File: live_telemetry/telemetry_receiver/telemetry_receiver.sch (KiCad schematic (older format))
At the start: 21 parts, among them J1 Conn_Coaxial, J2 Programming Header, J3 USB_A, U1 PIC16LF1455, U2 RFM95W, U3 AP2114H-3.3

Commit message: Add initial PCB layouts
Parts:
- J1: footprint (none) -> canhw_footprints:AmphenolRF_coaxial_conn_901-10510-2
- R5: footprint (none) -> Resistor_SMD:R_0805_2012Metric_Pad1.15x1.40mm_HandSolder
- U1: footprint (none) -> Package_SO:SOIC-14_3.9x8.7mm_P1.27mm
- U2: footprint (none) -> canhw_footprints:XCVR_RFM95W-915S2
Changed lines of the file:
@@
 F 0 "U1" H 4675 5115 50  0000 C CNN
 F 1 "PIC16LF1455" H 4675 5024 50  0000 C CNN
-F 2 "" H 4450 4800 50  0001 C CNN
+F 2 "Package_SO:SOIC-14_3.9x8.7mm_P1.27mm" H 4450 4800 50  0001 C CNN
 F 3 "http://ww1.microchip.com/downloads/en/DeviceDoc/40001639B.pdf" H 4450 4800 50  0001 C CNN
 	1    4450 4800
@@
 F 0 "U2" H 9000 4665 50  0000 C CNN
 F 1 "RFM95W" H 9000 4574 50  0000 C CNN
-F 2 "" H 8550 4550 50  0001 C CNN
+F 2 "canhw_footprints:XCVR_RFM95W-915S2" H 8550 4550 50  0001 C CNN
 F 3 "https://www.rfsolutions.co.uk/downloads/1463993415RFM95_96_97_98W.pdf" H 8550 4550 50  0001 C CNN
 	1    8500 3150
@@
 F 0 "J1" V 9782 2450 50  0000 L CNN
 F 1 "Conn_Coaxial" V 9873 2450 50  0000 L CNN
-F 2 "" H 9900 2350 50  0001 C CNN
+F 2 "canhw_footprints:AmphenolRF_coaxial_conn_901-10510-2" H 9900 2350 50  0001 C CNN
 F 3 " ~" H 9900 2350 50  0001 C CNN
 	1    9900 2350
@@
 F 0 "R5" H 3218 5396 50  0000 L CNN
 F 1 "10k" H 3218 5305 50  0000 L CNN
-F 2 "" V 3190 5340 50  0001 C CNN
+F 2 "Resistor_SMD:R_0805_2012Metric_Pad1.15x1.40mm_HandSolder" V 3190 5340 50  0001 C CNN
 F 3 "~" H 3150 5350 50  0001 C CNN
 	1    3150 5350

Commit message: Address Aaron's comments on initial component layout
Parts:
- J1: footprint canhw_footprints:AmphenolRF_coaxial_conn_901-10510-2 -> canhw_footprints:RF_connector_SMA_3-1478978-1
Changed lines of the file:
@@
 F 0 "J1" V 9782 2450 50  0000 L CNN
 F 1 "Conn_Coaxial" V 9873 2450 50  0000 L CNN
-F 2 "canhw_footprints:AmphenolRF_coaxial_conn_901-10510-2" H 9900 2350 50  0001 C CNN
+F 2 "canhw_footprints:RF_connector_SMA_3-1478978-1" H 9900 2350 50  0001 C CNN
 F 3 " ~" H 9900 2350 50  0001 C CNN
 	1    9900 2350

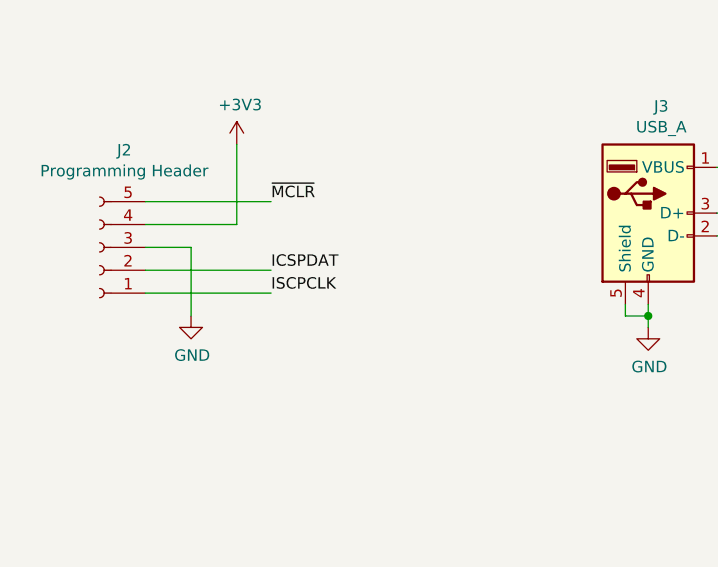
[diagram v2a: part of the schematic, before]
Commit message: Add initial trace routing
Note:
-LED colours still need to be added
-Waterloo Rocketry logo needs to be added with the board name and
my name on the right side of the board
-Copper pours will be added next commit
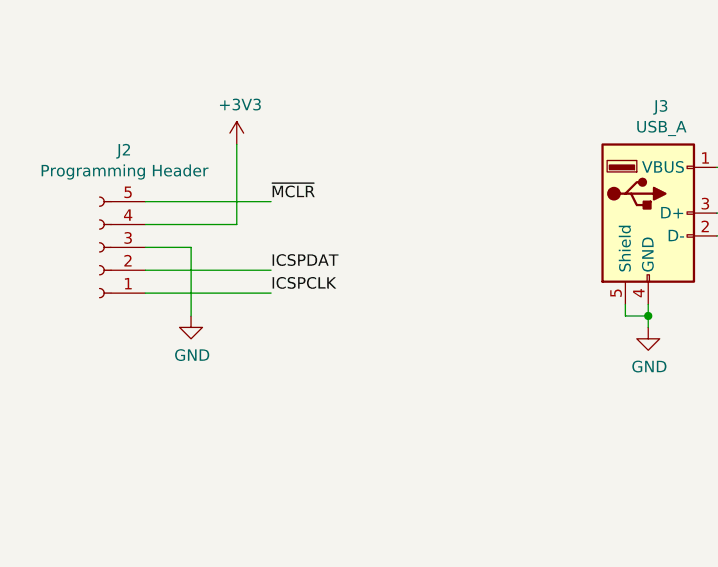
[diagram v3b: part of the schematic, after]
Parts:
- J2: footprint Connector_PinHeader_2.54mm:PinHeader_1x05_P2.54mm_Horizontal -> Connector_PinSocket_2.54mm:PinSocket_1x05_P2.54mm_Horizontal
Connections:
- net labels removed: ISCPCLK
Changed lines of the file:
@@
 F 0 "J2" H 1792 1875 50  0000 C CNN
 F 1 "Programming Header" H 1792 1966 50  0000 C CNN
-F 2 "Connector_PinHeader_2.54mm:PinHeader_1x05_P2.54mm_Horizontal" H 1900 2300 50  0001 C CNN
+F 2 "Connector_PinSocket_2.54mm:PinSocket_1x05_P2.54mm_Horizontal" H 1900 2300 50  0001 C CNN
 F 3 "~" H 1900 2300 50  0001 C CNN
 	1    1900 2300
@@
 ICSPDAT
 Text Label 2650 2500 0    50   ~ 0
-ISCPCLK
+ICSPCLK
 Wire Wire Line
 	2650 2500 2100 2500

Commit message: Remove old/replaced components for LTT and LTR
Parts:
- removed U1: PIC16LF1455, Package_SO:SOIC-14_3.9x8.7mm_P1.27mm, symbol canhw:PIC16F1455
- removed U2: RFM95W, canhw_footprints:XCVR_RFM95W-915S2, symbol canhw:RFM95W
- removed U3: AP2114H-3.3, Package_TO_SOT_SMD:SOT-23-5_HandSoldering, symbol Regulator_Linear:AP2112K-3.3
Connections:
- no-connect marks 6 -> 0

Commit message: Add LTR PIC and update LTR LDO
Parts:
- removed C2: 0.1u, Capacitor_SMD:C_0805_2012Metric_Pad1.15x1.40mm_HandSolder, symbol Device:C
- removed C4: 0.47u, Capacitor_SMD:C_0805_2012Metric_Pad1.15x1.40mm_HandSolder, symbol Device:C
- removed R5: 10k, Resistor_SMD:R_0805_2012Metric_Pad1.15x1.40mm_HandSolder, symbol Device:R_US
- added U?: PIC18F97J94, symbol canhw:PIC18F97J94
- added U?: NCV8114ASN330T1G, Package_TO_SOT_SMD:TSOT-23-5, symbol Regulator_Linear:NCV8114ASN330T1G
- C5, C6: value 4.7u -> 1u
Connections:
- net labels added: +3.3V
- wire segments 88 -> 81
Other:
- note removed: "NOTE: The MOSI and SCK SPI lines are sharing pins 9 and 10 with ICSPCLK and ICSPDAT. \nThis will prevent the board from using the PIC in-circuit debugging and sending data over\nserial at the same time. However, this solution is currently being used by USB board, and is\nwhat is recommended to be done in order to communicate with SPI with this specific PIC chip."
- moved on the sheet: C1, C3, C5, C6, D1, D2, D3, J2, J3, R1, R2, R3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

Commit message: Remove unused parts from LTS and add in new LTR MCU
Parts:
- removed AE1: Antenna, symbol Device:Antenna
- removed C1: 100p, Capacitor_SMD:C_0805_2012Metric_Pad1.15x1.40mm_HandSolder, symbol Device:C
- removed C3: 0.1u, Capacitor_SMD:C_0805_2012Metric_Pad1.15x1.40mm_HandSolder, symbol Device:C
- removed C5, C6: 1u, Capacitor_SMD:C_0805_2012Metric_Pad1.15x1.40mm_HandSolder, symbol Device:C
- removed J1: Conn_Coaxial, canhw_footprints:RF_connector_SMA_3-1478978-1, symbol Connector:Conn_Coaxial
- removed J3: USB_A, Connector_USB:USB_A_CNCTech_1001-011-01101_Horizontal, symbol Connector:USB_A
- removed U?: NCV8114ASN330T1G, Package_TO_SOT_SMD:TSOT-23-5, symbol Regulator_Linear:NCV8114ASN330T1G
- added C? (x2): C, symbol Device:C
- added Y?: Crystal, symbol Device:Crystal
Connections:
- net labels added: OSC1, OSC2
- net labels removed: +5V, MISO, MOSI, RESET, SCK, ~SS
- wire segments 81 -> 50
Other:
- moved on the sheet: D1, D2, D3, J2, R1, R2, R3, R4

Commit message: Add radios and label LTT and LTR
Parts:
- added C? (x2): 1u, Capacitor_SMD:C_0805_2012Metric_Pad1.15x1.40mm_HandSolder, symbol Device:C
- added C? (x2): 0.1uF, symbol Device:C
- added J?: USB_A, Connector_USB:USB_A_CNCTech_1001-011-01101_Horizontal, symbol Connector:USB_A
- added U?: ?, Package_TO_SOT_SMD:TSOT-23-5, symbol Regulator_Linear:NCV8114ASN330T1G
- C? (x2): value C -> 27pF
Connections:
- net labels added: +5V
- net labels removed: VUSB3V3
- wire segments 50 -> 79
- no-connect marks 0 -> 40
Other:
- note added: "12 MHz CRYSTAL"
- note added: "5V to 3.3V VOLTAGE REGULATOR"
- note added: "DEBUG LEDS"
- note added: "MCU"
- note added: "PROGRAMMING HEADER"
- note added: "USB CONNECTOR"
- moved on the sheet: J2

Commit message: Add placeholder LDOs for LTT and LTR
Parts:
- C? (x2): value 1u -> 1uF
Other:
- note added: "Note: The actual voltage regulator part # has not been selected yet. TBD ASAP."
- note added: "Note: This PIC has lots of unused pins,\nbut not many PICs had USB support. \nThis PIC also has CAN support for \npotential future CAN debugging on LTR."
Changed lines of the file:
@@
 encoding utf-8
 Sheet 1 2
-Title ""
-Date ""
-Rev ""
+Title "Live Telemetry Receiver"
+Date "2021-09-27"
+Rev "2.0"
 Comp ""
 Comment1 ""
@@
 AR Path="/6109AF45/61564D33" Ref="C?"  Part="1"
 F 0 "C?" H 9065 3646 50  0000 L CNN
-F 1 "1u" H 9065 3555 50  0000 L CNN
+F 1 "1uF" H 9065 3555 50  0000 L CNN
 F 2 "Capacitor_SMD:C_0805_2012Metric_Pad1.15x1.40mm_HandSolder" H 8988 3450 50  0001 C CNN
 F 3 "~" H 8950 3600 50  0001 C CNN
@@
 AR Path="/6109AF45/61564D39" Ref="C?"  Part="1"
 F 0 "C?" H 10665 3646 50  0000 L CNN
-F 1 "1u" H 10665 3555 50  0000 L CNN
+F 1 "1uF" H 10665 3555 50  0000 L CNN
 F 2 "Capacitor_SMD:C_0805_2012Metric_Pad1.15x1.40mm_HandSolder" H 10588 3450 50  0001 C CNN
 F 3 "~" H 10550 3600 50  0001 C CNN
@@
 Text Notes 4350 5900 0    50   ~ 10
 MCU
+Text Notes 6900 1700 0    50   ~ 0
+Note: This PIC has lots of unused pins,\nbut not many PICs had USB support. \nThis PIC also has CAN support for \npotential future CAN debugging on LTR.
+Text Notes 8100 3050 0    50   ~ 10
+Note: The actual voltage regulator part # has not been selected yet. TBD ASAP.
 $EndSCHEMATC
